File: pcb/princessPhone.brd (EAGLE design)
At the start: 80.7 x 51.5 mm, 78 parts, among them P1 TC2030-MCP-NL, Q1 2N7002K, SW1 LL1105BF250Q, SW2 LL1105BF250Q, SW3 LL1105BF250Q, U1 Value, U2 AG1170-S3-VERTICAL, U3 PI32MX170D-PT, U4 BLUETOOTH-RN-52, X1 USB_MICRO_B, X3 XRJK-S-01-6-4-0-9M2

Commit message: FINISHED ROUTING
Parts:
- removed RED: YELLOW, led:CHIPLED_0603
- added LED7: GREEN, led:CHIPLED_0603
- LED3, LED5: value GREEN -> RED
- LED4: value YELLOW -> BLUE
- LED6: value YELLOW -> GREEN
- SW1, SW2, SW3: value LL1105BF250Q -> (none); device raveGearControl:LL1105 -> switch-omron:B3F-31XX
- moved R29 62.2 mm to (-34.9, 7.01), turned to 180 degrees
- moved LED4 58.0 mm to (-38.1, 7.77), turned to 270 degrees
- moved SW1 53.7 mm to (-26.2, -22.2), turned to 0 degrees
- moved R27 52.7 mm to (-34.9, 11.0), turned to 180 degrees
- moved SW2 51.5 mm to (-16.1, -22.2), turned to 0 degrees
- moved R28 49.9 mm to (-34.9, 8.99), turned to 180 degrees
- moved SW3 49.5 mm to (-6.05, -22.2), turned to 0 degrees
- moved R8 48.7 mm to (-26.3, -20.9), turned to 0 degrees
- moved R9 46.3 mm to (-16.2, -20.9), turned to 0 degrees
- moved LED6 45.6 mm to (-38.1, 8.99), turned to 270 degrees
- moved LED5 45.2 mm to (-38.1, 10.2), turned to 270 degrees
- moved R10 44.1 mm to (-6.07, -20.9), turned to 0 degrees
- moved R19 15.7 mm to (-18.9, -2.39), turned to 270 degrees
- moved LED1 15.1 mm to (-24.6, -2.39), turned to 180 degrees
- moved LED2 15.0 mm to (-20.8, -2.39), turned to 180 degrees
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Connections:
- removed net +3V1: LED5.A
- net +3V3: now also LED4.A, LED5.A, LED6.A, LED7.A; no longer RED.A
- net N$12: now also LED7.C; no longer RED.C
- net PIC32_RSVD_1: now also R28.1
- net PIC32_RSVD_12: now also R27.1
- net PIC32_RSVD_2: now also R29.1
- net PIC32_RSVD_5: no longer R28.1, R29.1
- net PIC32_RSVD_8: no longer R27.1
- net SW0: now also SW1.2; no longer SW1.3
- net SW1: now also SW2.2; no longer SW2.3
- net SW2: now also SW3.2; no longer SW3.3
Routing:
- net SW0: track 0.00 -> 81.3 mm, vias 0 -> 2
- net SW1: track 0.00 -> 71.2 mm, vias 0 -> 2
- net USB_DM: track 0.00 -> 60.6 mm, vias 0 -> 3
- net SW2: track 0.00 -> 60.6 mm, vias 0 -> 2
- net AG1170_AUDIO_IN: track 2.84 -> 61.8 mm, vias 0 -> 1
- net USB_DP: track 0.00 -> 56.1 mm, vias 0 -> 3
- net AG1170_AUDIO_OUT: track 2.13 -> 46.9 mm, vias 0 -> 1
- net PIC32_RSVD_2: track 3.48 -> 47.6 mm, vias 0 -> 4
- net PIC32_RSVD_1: track 3.49 -> 23.2 mm, vias 0 -> 2
- net PIC32_RSVD_8: track 3.54 -> 21.7 mm
- net PIC32_RSVD_12: track 3.15 -> 20.2 mm
- net PIC32_RSVD_5: track 4.65 -> 20.7 mm
- net LED0: track 0.00 -> 14.5 mm, vias 0 -> 1
- net LED1: track 0.00 -> 11.1 mm, vias 0 -> 1
- net RN52_SPKR_L+: track 17.5 -> 6.72 mm
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
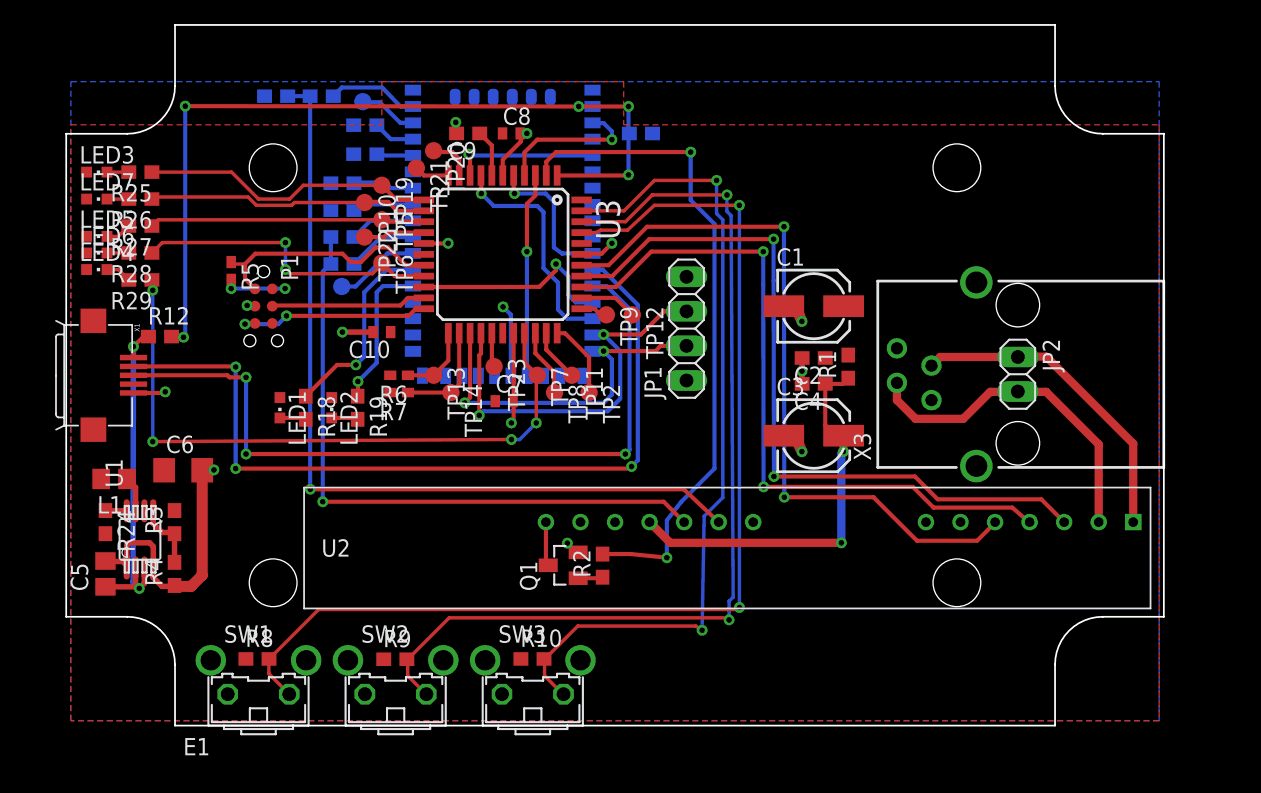
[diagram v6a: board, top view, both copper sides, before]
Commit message: UPDATED USB/RJ-11/OUTLINE
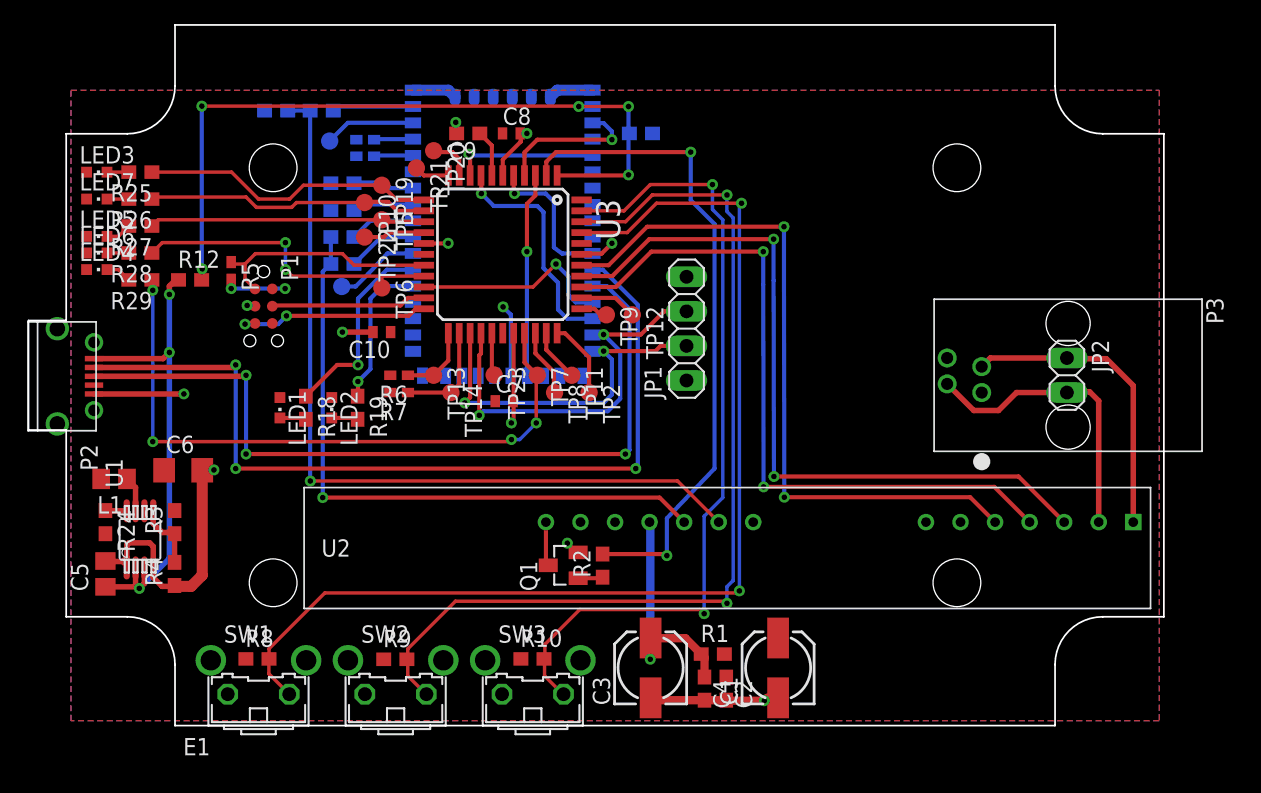
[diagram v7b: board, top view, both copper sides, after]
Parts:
- removed X1: USB_MICRO_B, FosBattery1:USB-MICROB
- removed X3: XRJK-S-01-6-4-0-9M2, con-xmultiple:XRJK-S-01-6-4-0-9M2
- added P2: 10118194, console_board:10118194
- added P3: 95009-7441, princessPhone:95009-7441
- E1: value 1591XXMS -> 1591XXMS-USB; device princessPhone:1591XXMSBK -> princessPhone:1591XXMSBK-USB
- R14, R15: device rcl:R0603 -> rcl:R0402
- moved C1 26.7 mm to (12.0, -21.5), turned to 90 degrees
- moved C2 25.1 mm to (8.18, -23.0), turned to 270 degrees
- moved C4 23.8 mm to (6.58, -23.0), turned to 270 degrees
- moved R1 23.4 mm to (7.19, -20.5), turned to 0 degrees
- moved C3 20.9 mm to (2.62, -21.5), turned to 90 degrees
- moved R12 4.72 mm to (-31.2, 7.01)
- moved TP3 3.79 mm to (-21.0, 17.2)
- moved JP2 3.61 mm to (33.2, 0.00)
- moved TP6 1.83 mm to (-17.1, 6.43)
- moved R14 1.07 mm to (-18.4, 17.3)
- moved R22 1.07 mm to (-21.6, 19.5)
- moved R23 1.07 mm to (-24.9, 19.5)
- moved TP23 0.61 mm to (-8.89, 0.03)
- moved R15 0.15 mm to (-18.4, 16.1)
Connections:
- net GND: now also P2.5; no longer X1.GND
- net PHONE_RING: now also P3.3; no longer X3.3
- net PHONE_TIP: now also P3.2; no longer X3.2
- net USB_DM: now also P2.2; no longer X1.D-
- net USB_DP: now also P2.3; no longer X1.D+
- net USB_VBUS: now also P2.1; no longer X1.VBUS
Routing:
- net GND: track 49.4 -> 63.7 mm, vias 13 -> 11
- net +VA: track 29.2 -> 17.7 mm, vias 2 -> 1
- net USB_VBUS: track 26.2 -> 35.5 mm, vias 2 -> 3
- net RN52_DFU_MODE: track 61.9 -> 56.0 mm
- net USB_DM: track 60.6 -> 64.1 mm
- net PHONE_TIP: track 24.8 -> 21.7 mm
- net USB_DP: track 56.1 -> 59.1 mm
- net RN52_SPKR_R+: track 4.33 -> 6.68 mm
- net AG1170_AUDIO_IN: track 61.8 -> 60.2 mm
- net PHONE_RING: track 23.5 -> 22.3 mm
- net AG1170_SHK: track 53.4 -> 52.2 mm
- net MCLR#: track 17.9 -> 17.0 mm
- net RN52_SPKR_L+: track 6.72 -> 5.99 mm
- net SST25_MISO: track 2.52 -> 3.13 mm
- net SW2: track 60.6 -> 60.1 mm
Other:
- board size 80.7 x 51.5 mm -> 83.5 x 51.5 mm
- board text added: ">DRAWING_NAME"
- board text added: "RING"
- board text added: "Rev A"
- board text added: "TIP"

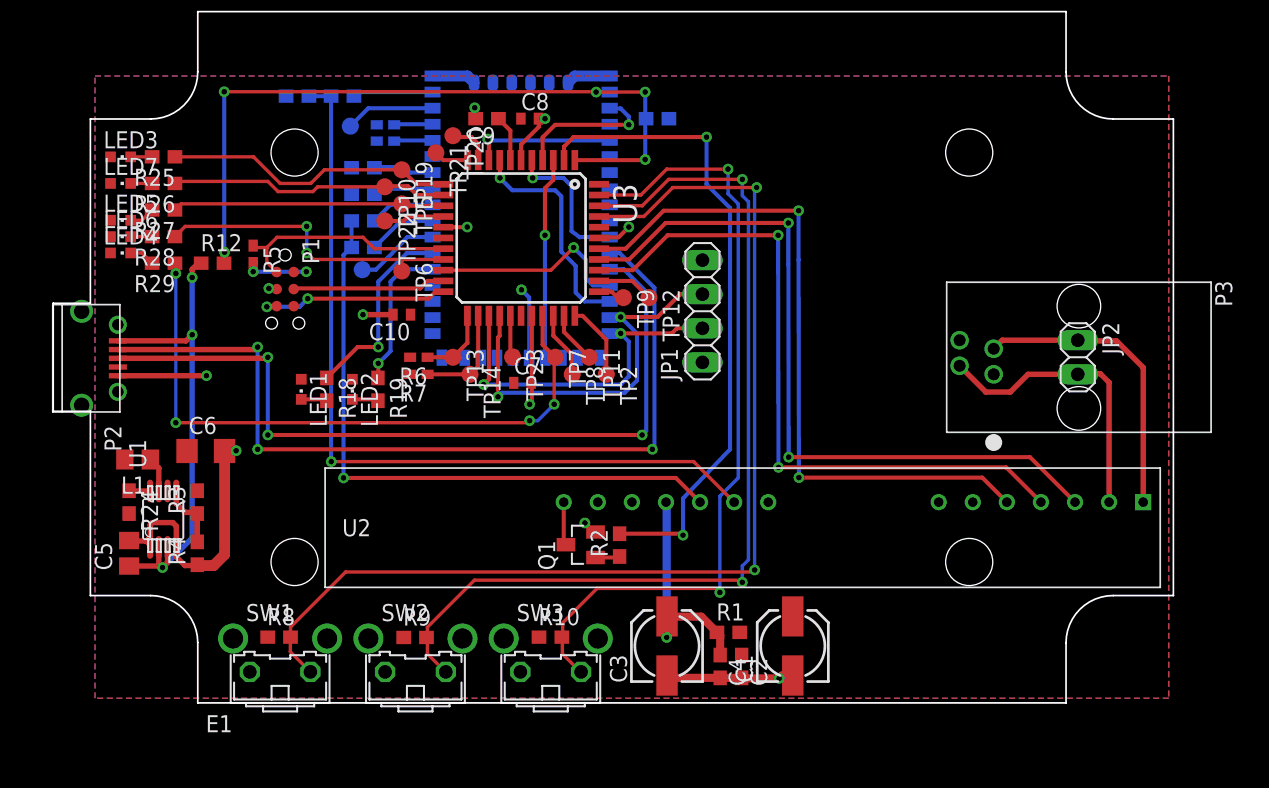
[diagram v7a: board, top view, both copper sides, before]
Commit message: Replaced placeholder components with proper ones.
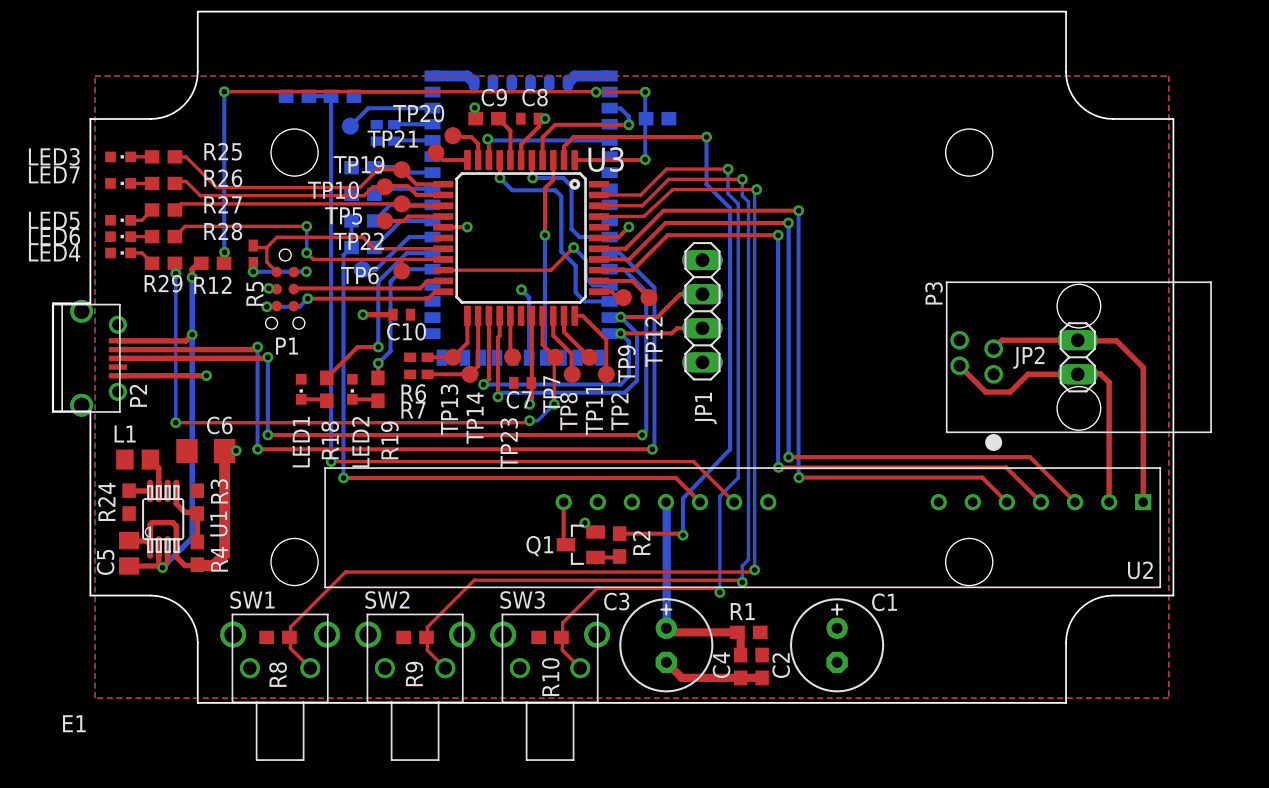
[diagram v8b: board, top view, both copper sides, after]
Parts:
- C1, C3: device rcl:153CLV-0505 -> rcl:E2,5-7
- SW1, SW2, SW3: value (none) -> TL1105; device switch-omron:B3F-31XX -> princessPhone:TL1105_RA
- moved C1 3.30 mm to (15.3, -21.5), turned to 270 degrees
- moved C4 1.52 mm to (8.10, -23.0)
- moved C2 1.52 mm to (9.70, -23.0)
- moved R1 1.52 mm to (8.71, -20.5)
- moved SW3 0.97 mm to (-6.10, -23.2)
- moved SW2 0.97 mm to (-16.2, -23.2)
- moved SW1 0.97 mm to (-26.2, -23.2)
- moved R8 0.08 mm to (-26.4, -20.9)
- moved C3 0.07 mm to (2.57, -21.5), turned to 270 degrees
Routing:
- net GND: track 63.7 -> 61.8 mm, vias 11 -> 10
- net +VA: track 17.7 -> 16.6 mm, vias 1 -> 0
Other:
- board text added: "3V3"
- board text added: "GND"
- board text added: "RX"
- board text added: "TX"
